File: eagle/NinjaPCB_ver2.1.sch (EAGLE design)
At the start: 58 parts, among them IC3 ANALOGSW_AD_SOT23-6, IC6 NAU7802, J2 ATX24, J3 HEATER, J4 HEATER_TEMP, Q1 S8550, Q2 IRF520NPBF, Q3 IRF520NPBF, Q4 S8550, Q5 IRF520NPBF, Q6 S8550, Q7 S8550, Q8 S8550, U1 CJT1117-3.3-SOT223

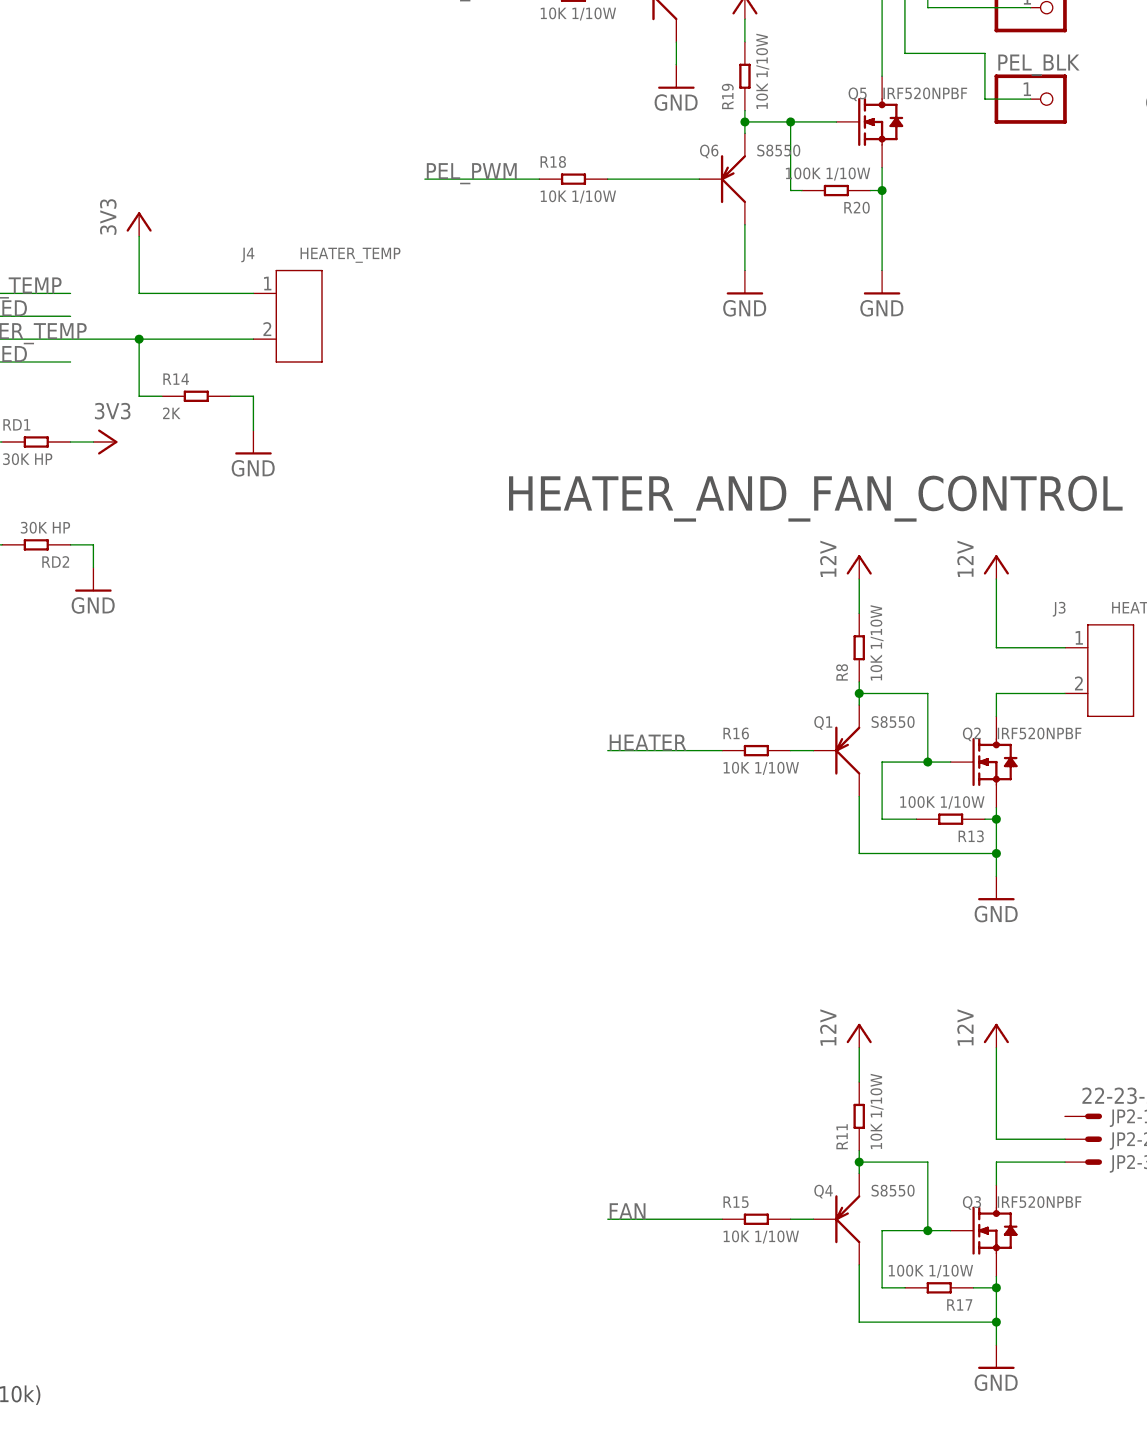
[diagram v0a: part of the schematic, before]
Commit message: use easier parts. add notes to design
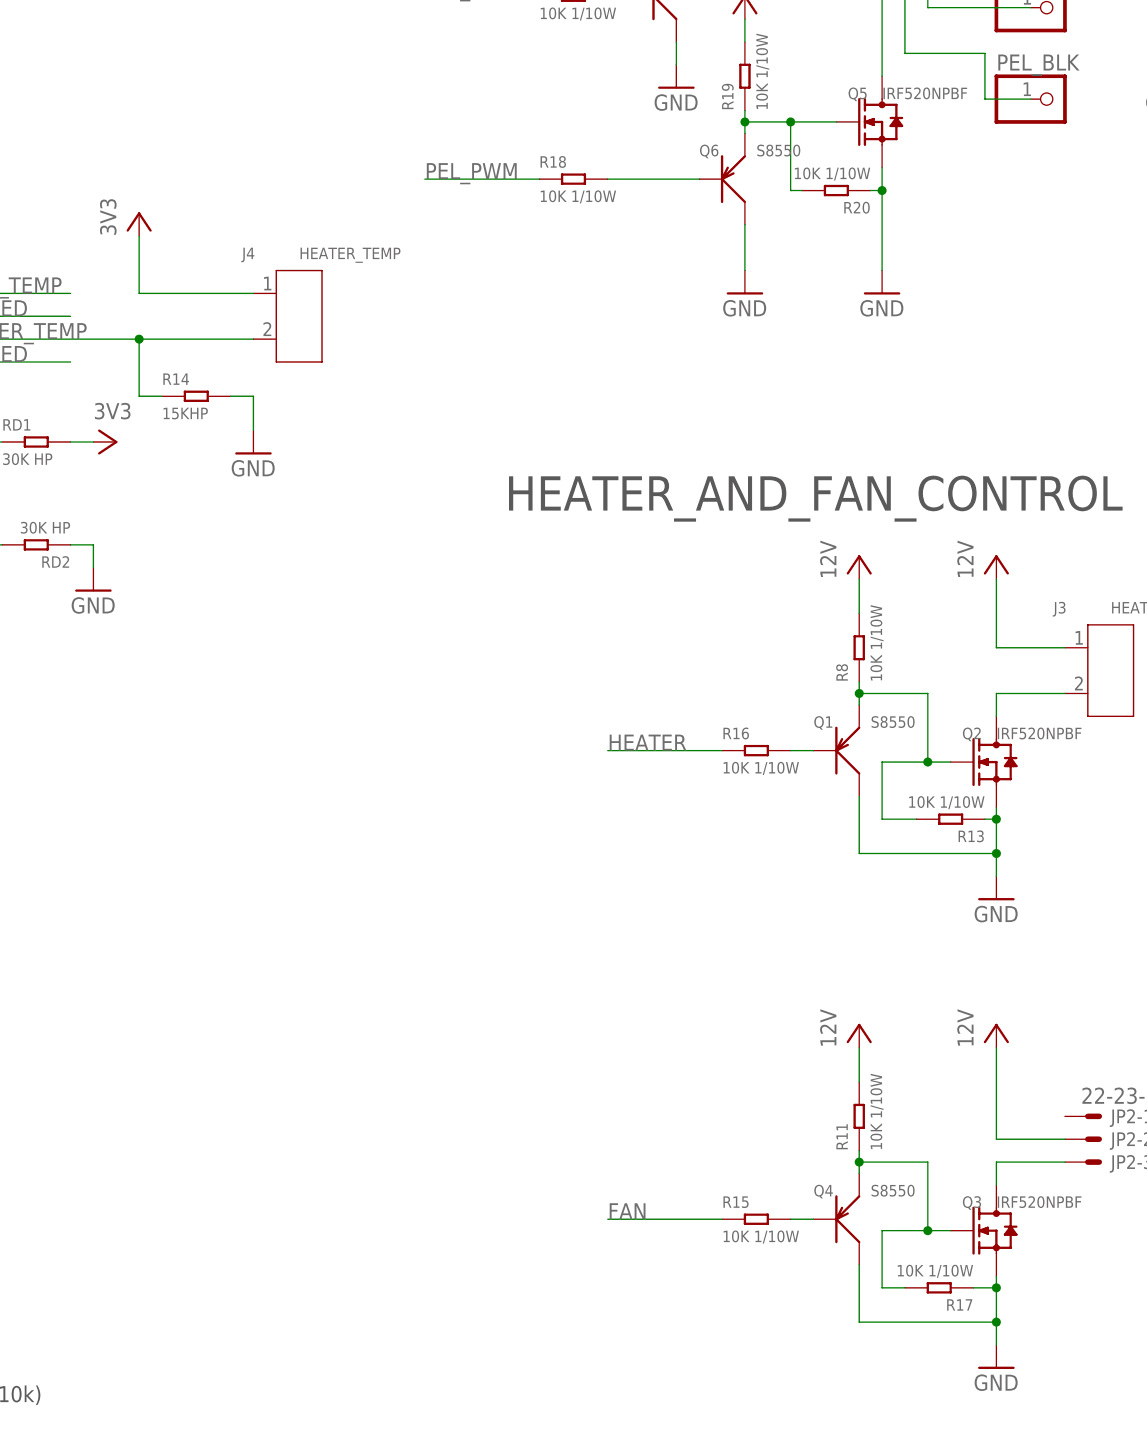
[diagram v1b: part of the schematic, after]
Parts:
- R13, R17, R20: value 100K 1/10W -> 10K 1/10W; device Seeed-Resistor:SMD-RES-100K-5%-1/10W(0603) -> Seeed-Resistor:SMD-RES-10K-5%-1/10W(0603)
- R14: value 2K -> 15KHP

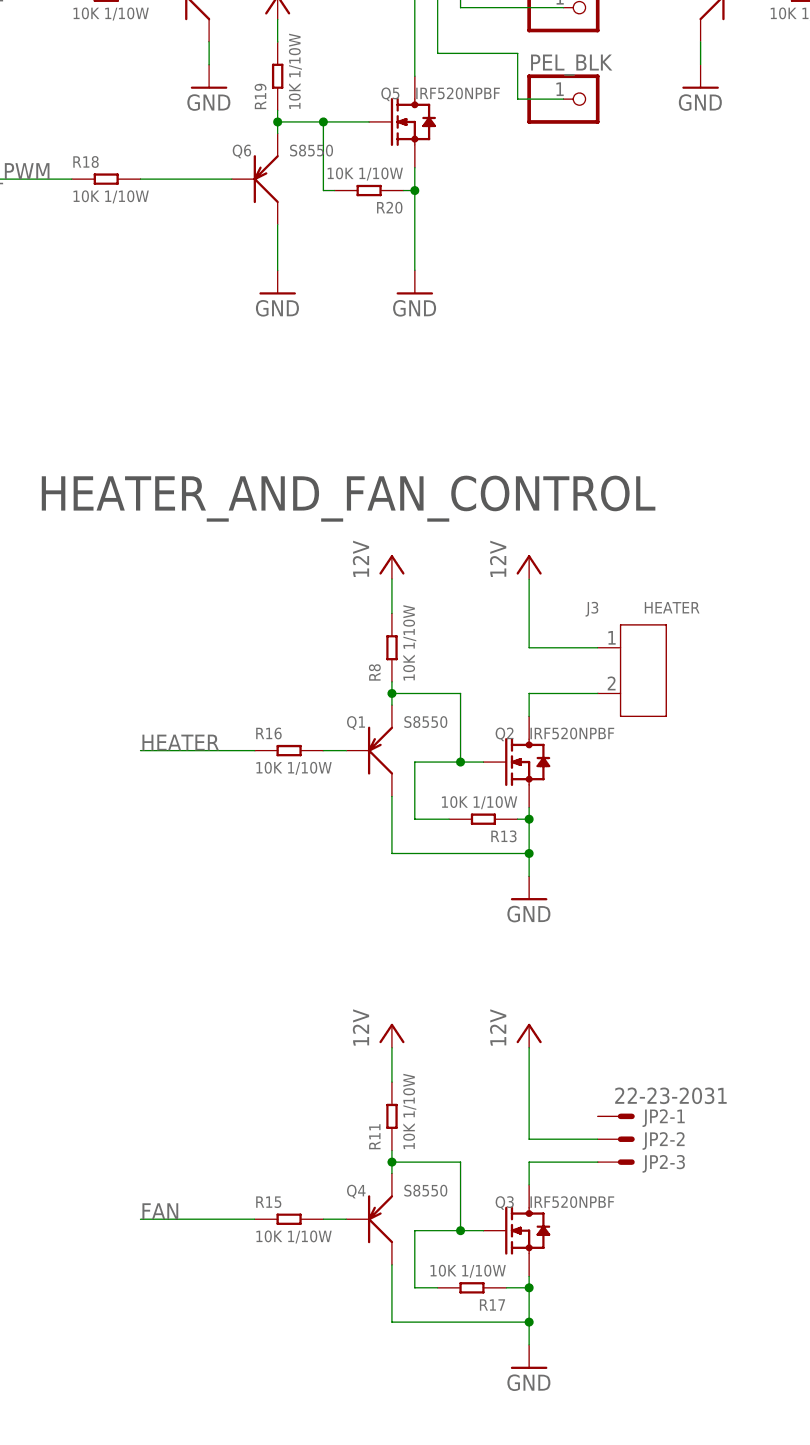
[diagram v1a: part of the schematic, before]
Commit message: change values of MOSFET G-S reg
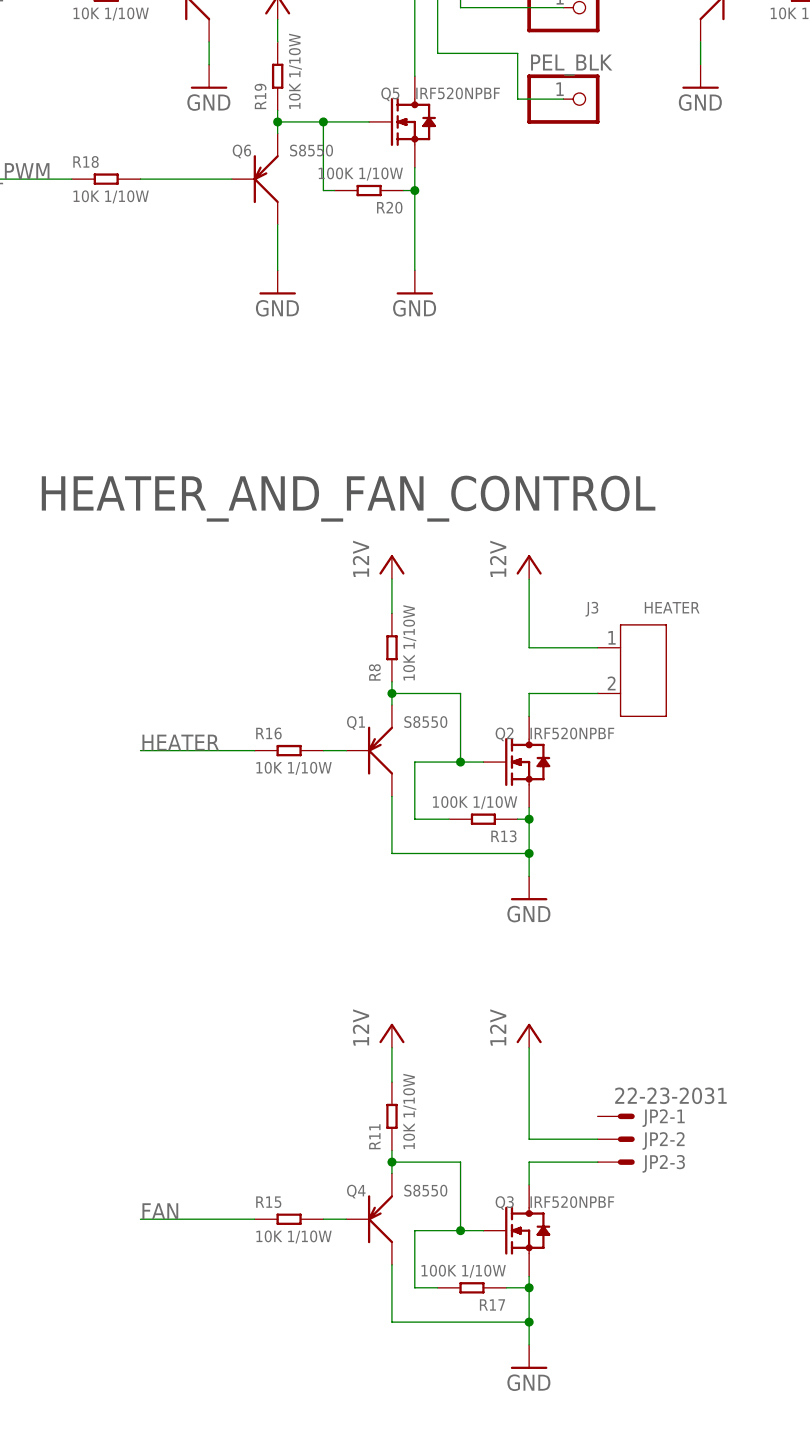
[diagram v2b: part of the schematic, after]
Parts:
- R13, R17, R20: value 10K 1/10W -> 100K 1/10W; device Seeed-Resistor:SMD-RES-10K-5%-1/10W(0603) -> Seeed-Resistor:SMD-RES-100K-5%-1/10W(0603)
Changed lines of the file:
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@@
 <grid distance="0.1" unitdist="inch" unit="inch" style="lines" multiple="1" display="no" altdistance="0.01" altunitdist="inch" altunit="inch"/>
 <layers>
-<layer number="1" name="Top" color="4" fill="1" visible="yes" active="no"/>
-<layer number="2" name="Route2" color="1" fill="3" visible="yes" active="no"/>
-<layer number="3" name="Route3" color="4" fill="3" visible="yes" active="no"/>
-<layer number="4" name="Route4" color="1" fill="4" visible="yes" active="no"/>
-<layer number="5" name="Route5" color="4" fill="4" visible="yes" active="no"/>
-<layer number="6" name="Route6" color="1" fill="8" visible="yes" active="no"/>
-<layer number="7" name="Route7" color="4" fill="8" visible="yes" active="no"/>
-<layer number="8" name="Route8" color="1" fill="2" visible="yes" active="no"/>
-<layer number="9" name="Route9" color="4" fill="2" visible="yes" active="no"/>
-<layer number="10" name="Route10" color="1" fill="7" visible="yes" active="no"/>
-<layer number="11" name="Route11" color="4" fill="7" visible="yes" active="no"/>
-<layer number="12" name="Route12" color="1" fill="5" visible="yes" active="no"/>
-<layer number="13" name="Route13" color="4" fill="5" visible="yes" active="no"/>
-<layer number="14" name="Route14" color="1" fill="6" visible="yes" active="no"/>
-<layer number="15" name="Route15" color="4" fill="6" visible="yes" active="no"/>
-<layer number="16" name="Bottom" color="1" fill="1" visible="yes" active="no"/>
-<layer number="17" name="Pads" color="2" fill="1" visible="yes" active="no"/>
-<layer number="18" name="Vias" color="2" fill="1" visible="yes" active="no"/>
-<layer number="19" name="Unrouted" color="6" fill="1" visible="yes" active="no"/>
-<layer number="20" name="Dimension" color="15" fill="1" visible="yes" active="no"/>
-<layer number="21" name="tPlace" color="7" fill="1" visible="yes" active="no"/>
-<layer number="22" name="bPlace" color="7" fill="1" visible="yes" active="no"/>
-<layer number="23" name="tOrigins" color="15" fill="1" visible="yes" active="no"/>
-<layer number="24" name="bOrigins" color="15" fill="1" visible="yes" active="no"/>
-<layer number="25" name="tNames" color="7" fill="1" visible="yes" active="no"/>
-<layer number="26" name="bNames" color="7" fill="1" visible="yes" active="no"/>
-<layer number="27" name="tValues" color="7" fill="1" visible="yes" active="no"/>
-<layer number="28" name="bValues" color="7" fill="1" visible="yes" active="no"/>
+<layer number="1" name="Top" color="4" fill="1" visible="no" active="no"/>
+<layer number="2" name="Route2" color="1" fill="3" visible="no" active="no"/>
+<layer number="3" name="Route3" color="4" fill="3" visible="no" active="no"/>
+<layer number="4" name="Route4" color="1" fill="4" visible="no" active="no"/>
+<layer number="5" name="Route5" color="4" fill="4" visible="no" active="no"/>
+<layer number="6" name="Route6" color="1" fill="8" visible="no" active="no"/>
+<layer number="7" name="Route7" color="4" fill="8" visible="no" active="no"/>
+<layer number="8" name="Route8" color="1" fill="2" visible="no" active="no"/>
+<layer number="9" name="Route9" color="4" fill="2" visible="no" active="no"/>
+<layer number="10" name="Route10" color="1" fill="7" visible="no" active="no"/>
+<layer number="11" name="Route11" color="4" fill="7" visible="no" active="no"/>
+<layer number="12" name="Route12" color="1" fill="5" visible="no" active="no"/>
+<layer number="13" name="Route13" color="4" fill="5" visible="no" active="no"/>
+<layer number="14" name="Route14" color="1" fill="6" visible="no" active="no"/>
+<layer number="15" name="Route15" color="4" fill="6" visible="no" active="no"/>
+<layer number="16" name="Bottom" color="1" fill="1" visible="no" active="no"/>
+<layer number="17" name="Pads" color="2" fill="1" visible="no" active="no"/>
+<layer number="18" name="Vias" color="2" fill="1" visible="no" active="no"/>
+<layer number="19" name="Unrouted" color="6" fill="1" visible="no" active="no"/>
+<layer number="20" name="Dimension" color="15" fill="1" visible="no" active="no"/>
+<layer number="21" name="tPlace" color="7" fill="1" visible="no" active="no"/>
+<layer number="22" name="bPlace" color="7" fill="1" visible="no" active="no"/>
+<layer number="23" name="tOrigins" color="15" fill="1" visible="no" active="no"/>
+<layer number="24" name="bOrigins" color="15" fill="1" visible="no" active="no"/>
+<layer number="25" name="tNames" color="7" fill="1" visible="no" active="no"/>
+<layer number="26" name="bNames" color="7" fill="1" visible="no" active="no"/>
+<layer number="27" name="tValues" color="7" fill="1" visible="no" active="no"/>
+<layer number="28" name="bValues" color="7" fill="1" visible="no" active="no"/>
 <layer number="29" name="tStop" color="7" fill="3" visible="no" active="no"/>
 <layer number="30" name="bStop" color="7" fill="6" visible="no" active="no"/>
@@
 <layer number="35" name="tGlue" color="7" fill="4" visible="no" active="no"/>
 <layer number="36" name="bGlue" color="7" fill="5" visible="no" active="no"/>
-<layer number="37" name="tTest" color="7" fill="1" visible="yes" active="no"/>
-<layer number="38" name="bTest" color="7" fill="1" visible="yes" active="no"/>
+<layer number="37" name="tTest" color="7" fill="1" visible="no" active="no"/>
+<layer number="38" name="bTest" color="7" fill="1" visible="no" active="no"/>
 <layer number="39" name="tKeepout" color="4" fill="11" visible="no" active="no"/>
 <layer number="40" name="bKeepout" color="1" fill="11" visible="no" active="no"/>
@@
 <layer number="44" name="Drills" color="7" fill="1" visible="no" active="no"/>
 <layer number="45" name="Holes" color="7" fill="1" visible="no" active="no"/>
-<layer number="46" name="Milling" color="3" fill="1" visible="yes" active="no"/>
-<layer number="47" name="Measures" color="7" fill="1" visible="yes" active="no"/>
-<layer number="48" name="Document" color="7" fill="1" visible="yes" active="no"/>
-<layer number="49" name="Reference" color="7" fill="1" visible="yes" active="no"/>
-<layer number="50" name="dxf" color="7" fill="1" visible="yes" active="no"/>
-<layer number="51" name="tDocu" color="7" fill="1" visible="yes" active="no"/>
-<layer number="52" name="bDocu" color="7" fill="1" visible="yes" active="no"/>
-<layer number="53" name="tGND_GNDA" color="7" fill="9" visible="yes" active="no"/>
-<layer number="54" name="bGND_GNDA" color="1" fill="9" visible="yes" active="no"/>
-<layer number="56" name="wert" color="7" fill="1" visible="yes" active="no"/>
-<layer number="57" name="tCAD" color="7" fill="1" visible="yes" active="no"/>
-<layer number="59" name="tCarbon" color="7" fill="1" visible="yes" active="no"/>
-<layer number="60" name="bCarbon" color="7" fill="1" visible="yes" active="no"/>
+<layer number="46" name="Milling" color="3" fill="1" visible="no" active="no"/>
+<layer number="47" name="Measures" color="7" fill="1" visible="no" active="no"/>
+<layer number="48" name="Document" color="7" fill="1" visible="no" active="no"/>
+<layer number="49" name="Reference" color="7" fill="1" visible="no" active="no"/>
+<layer number="50" name="dxf" color="7" fill="1" visible="no" active="no"/>
+<layer number="51" name="tDocu" color="7" fill="1" visible="no" active="no"/>
+<layer number="52" name="bDocu" color="7" fill="1" visible="no" active="no"/>
+<layer number="53" name="tGND_GNDA" color="7" fill="9" visible="no" active="no"/>
+<layer number="54" name="bGND_GNDA" color="1" fill="9" visible="no" active="no"/>
+<layer number="56" name="wert" color="7" fill="1" visible="no" active="no"/>
+<layer number="57" name="tCAD" color="7" fill="1" visible="no" active="no"/>
+<layer number="59" name="tCarbon" color="7" fill="1" visible="no" active="no"/>
+<layer number="60" name="bCarbon" color="7" fill="1" visible="no" active="no"/>
 <layer number="90" name="Modules" color="5" fill="1" visible="yes" active="yes"/>
 <layer number="91" name="Nets" color="2" fill="1" visible="yes" active="yes"/>
@@
 <part name="R8" library="Seeed-Resistor" deviceset="SMD-RES-10K-5%-1/10W(0603)" device="" value="10K 1/10W"/>
 <part name="R11" library="Seeed-Resistor" deviceset="SMD-RES-10K-5%-1/10W(0603)" device="" value="10K 1/10W"/>
-<part name="R13" library="Seeed-Resistor" deviceset="SMD-RES-10K-5%-1/10W(0603)" device="" value="10K 1/10W"/>
-<part name="R17" library="Seeed-Resistor" deviceset="SMD-RES-10K-5%-1/10W(0603)" device="" value="10K 1/10W"/>
+<part name="R13" library="Seeed-Resistor" deviceset="SMD-RES-100K-5%-1/10W(0603)" device="" value="100K 1/10W"/>
+<part name="R17" library="Seeed-Resistor" deviceset="SMD-RES-100K-5%-1/10W(0603)" device="" value="100K 1/10W"/>
 <part name="Q5" library="Seeed-Transistor" deviceset="DIP-MOSFET-N-CH-100V-9.7A-IRF520NPBF(TO-220AB)" device="CORRECT" value="IRF520NPBF"/>
 <part name="GND3" library="supply1" deviceset="GND" device=""/>
@@
 <part name="Q6" library="Seeed-Transistor" deviceset="SMD-TRANSISTORS-PNP-25V-500MA-S8550(SOT-23)" device="" value="S8550"/>
 <part name="R19" library="Seeed-Resistor" deviceset="SMD-RES-10K-5%-1/10W(0603)" device="" value="10K 1/10W"/>
-<part name="R20" library="Seeed-Resistor" deviceset="SMD-RES-10K-5%-1/10W(0603)" device="" value="10K 1/10W"/>
+<part name="R20" library="Seeed-Resistor" deviceset="SMD-RES-100K-5%-1/10W(0603)" device="" value="100K 1/10W"/>
 <part name="RELAY" library="PCR-Switch" deviceset="NEC-RELAY2" device="ET2"/>
 <part name="D1" library="Seeed-Diode" deviceset="DIODE-GEN-PURPOSE-1KV-1A(DO-214AC)" device="" value="1N4007"/>
